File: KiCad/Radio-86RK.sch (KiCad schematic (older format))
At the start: 17 parts, among them SW67 Reset, U1 8080A/КР580ВМ80А, U12 74LS373/К555ИР22, U14 74LS138/К555ИД7, U16 7486/К155ЛП5, U17 7474/К155ТМ2, U18 7408/К155ЛИ1, U19 7404/К155ЛН1, U2 8224/КР580ГФ24, U20 7400/К155ЛА3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

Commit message: Change 8224 package to DIP16; Swap Down/Right keys; Fix U21 soviet designation
Signed-off-by: Sergey Kiselev <skiselev@gmail.com>
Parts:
- U2: footprint My_Components:IC_DIP20_300 -> My_Components:IC_DIP16_300
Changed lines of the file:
@@
 F 0 "U2" H 2100 2450 60  0000 L CNN
 F 1 "8224/КР580ГФ24" H 1600 2350 60  0000 L CNN
-F 2 "My_Components:IC_DIP20_300" H 2500 1600 60  0001 C CNN
+F 2 "My_Components:IC_DIP16_300" H 2500 1600 60  0001 C CNN
 F 3 "" H 2500 1600 60  0000 C CNN
 	1    2500 1650
@@
 Wire Wire Line
 	1700 1400 1800 1400
+$Comp
+L Device:C C44
+U 1 1 5F448F09
+P 1550 1400
+F 0 "C44" V 1600 1200 50  0000 L CNN
+F 1 "10pF" V 1600 1450 50  0000 L CNN
+F 2 "My_Components:Cap_Cer_508" H 1588 1250 50  0001 C CNN
+F 3 "" H 1550 1400 50  0000 C CNN
+	1    1550 1400
+	0    1    1    0
+$EndComp
 Wire Bus Line
-	9800 4600 9800 6100
+	6300 900  6300 4400
 Wire Bus Line
 	3400 4400 3400 5200
@@
 	4300 4500 4300 5700
 Wire Bus Line
-	6300 900  6300 4400
+	6100 2900 6100 4500
+Wire Bus Line
+	9800 4600 9800 6100
 Wire Bus Line
 	6100 900  6100 2500
-Wire Bus Line
-	6100 2900 6100 4500
-$Comp
-L Device:C C44
-U 1 1 5F448F09
-P 1550 1400
-F 0 "C44" V 1600 1200 50  0000 L CNN
-F 1 "10pF" V 1600 1450 50  0000 L CNN
-F 2 "My_Components:Cap_Cer_508" H 1588 1250 50  0001 C CNN
-F 3 "" H 1550 1400 50  0000 C CNN
-	1    1550 1400
-	0    1    1    0
-$EndComp
 $EndSCHEMATC

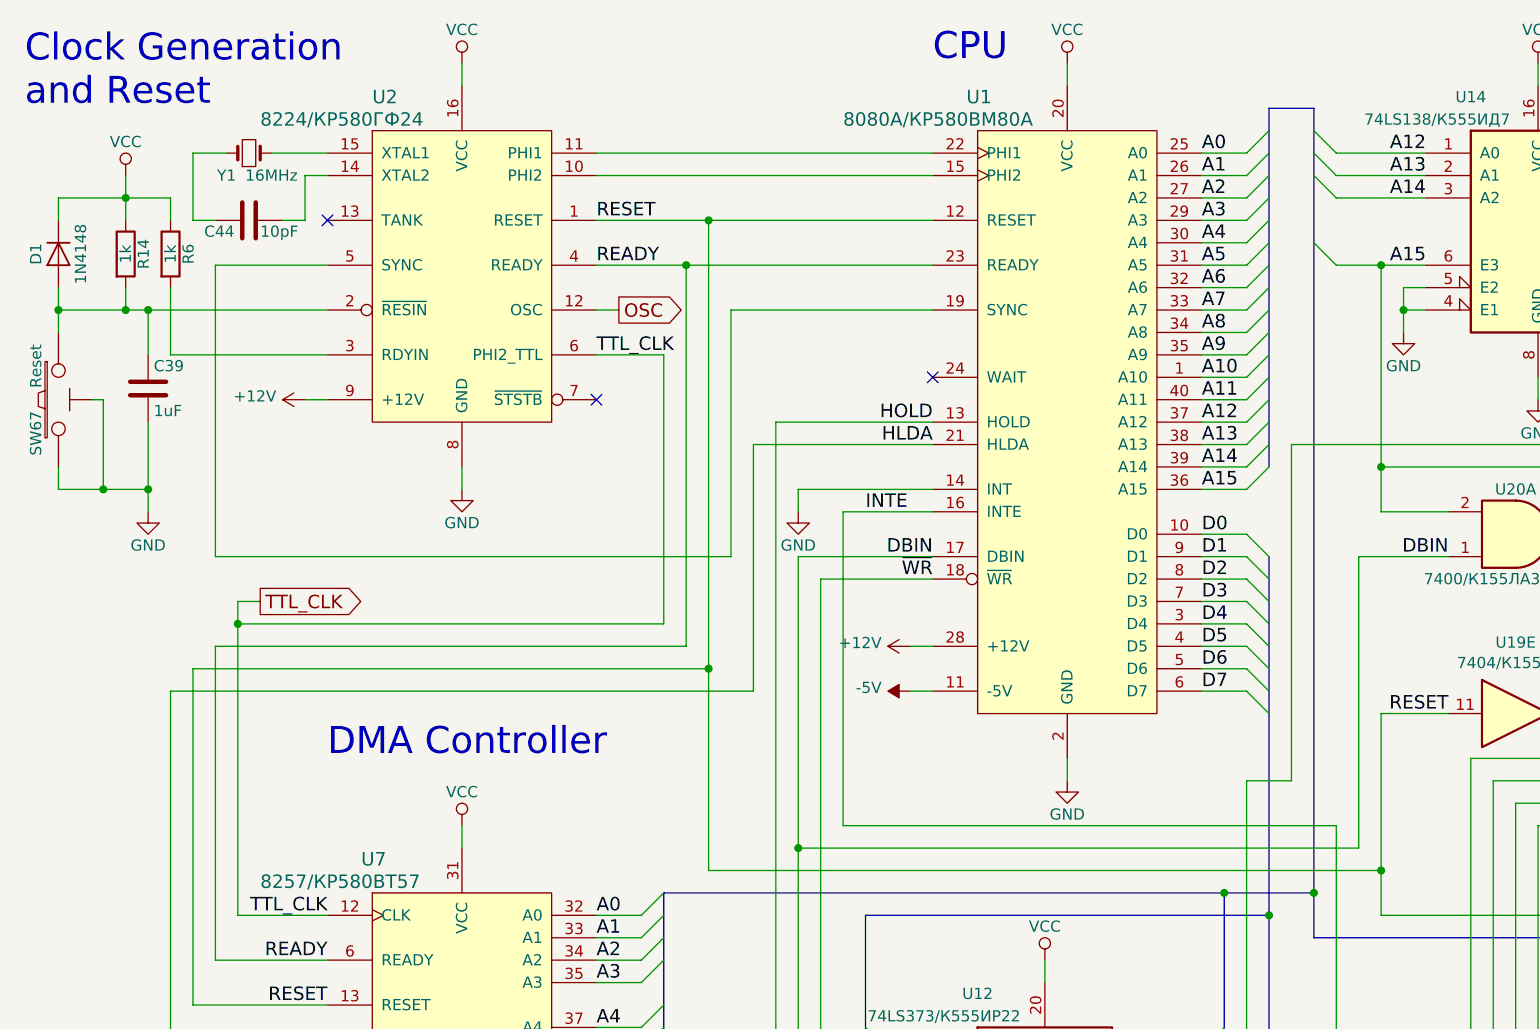
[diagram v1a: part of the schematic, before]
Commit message: Use DS1233 for reset
Signed-off-by: Sergey Kiselev <skiselev@gmail.com>
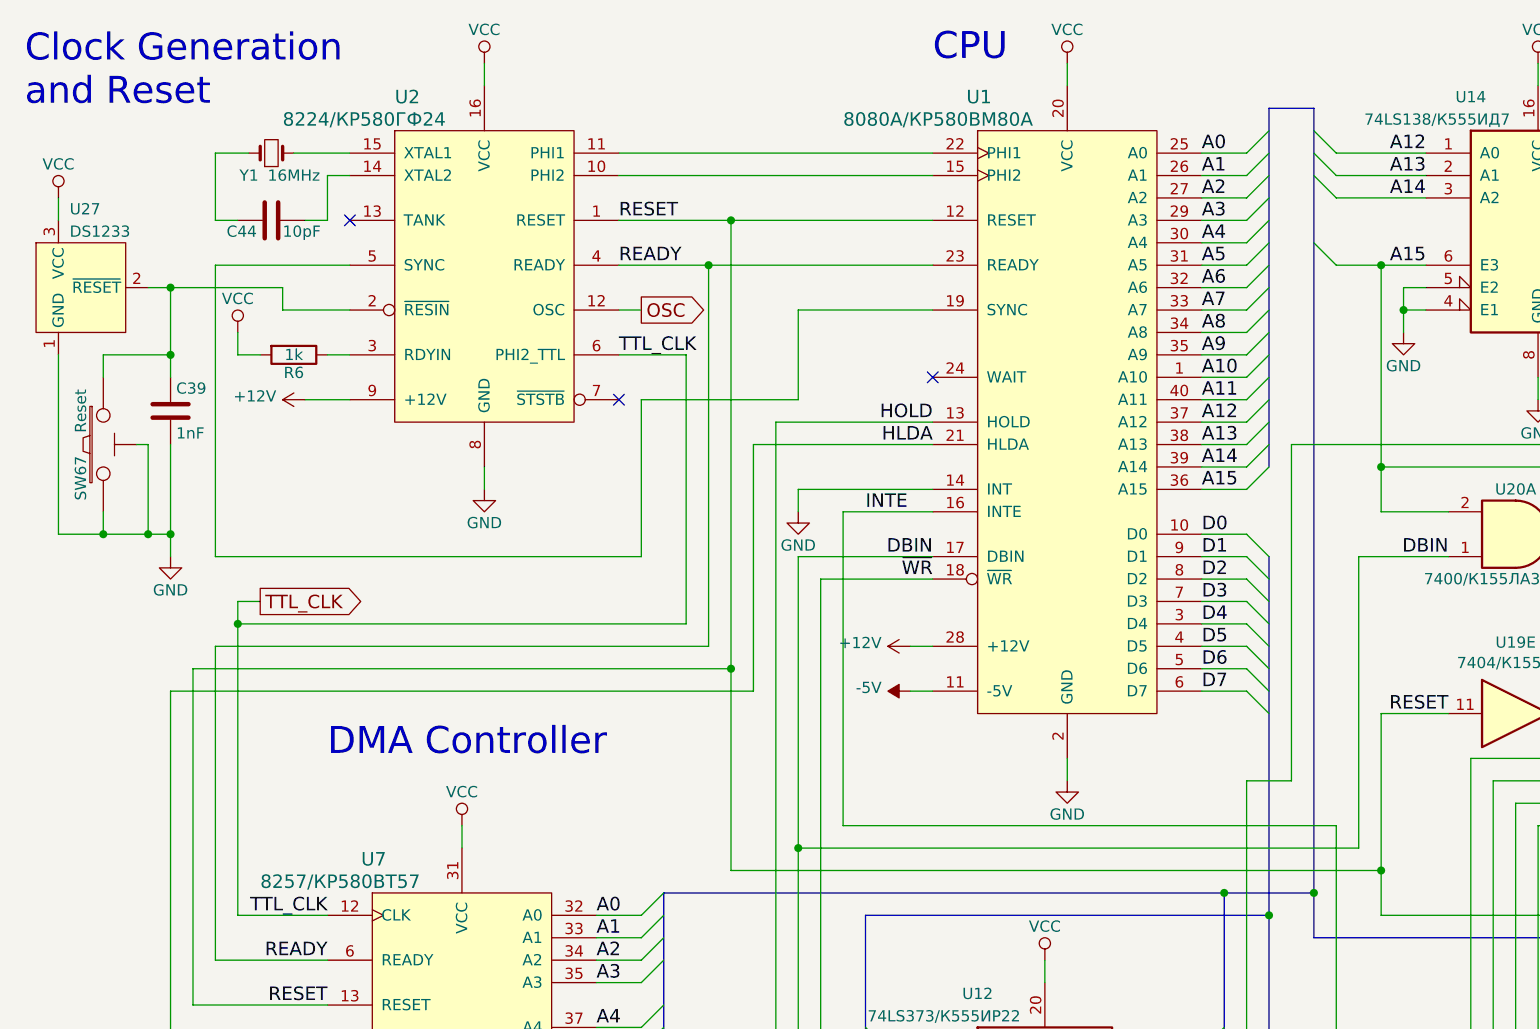
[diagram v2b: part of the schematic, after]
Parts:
- removed D1: 1N4148, My_Components:Diode_762, symbol Device:D
- removed R14: 1k, My_Components:Res_762, symbol Device:R
- added U27: DS1233, My_Components:Transistor_TO92_EBC_254, symbol my_components:DS1233
- C39: value 1uF -> 1nF
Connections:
- net GND: now also U27.1 (GND)
- net VCC: now also R6.2, U27.3 (VCC); no longer R6.1
- net at C39.1, SW67.1, U2.2 (~RESIN): now also U27.2 (~RESET)
- net at U2.3 (RDYIN): now also R6.1; no longer R6.2
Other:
- moved on the sheet: C39, C44, R6, SW67, U2, Y1

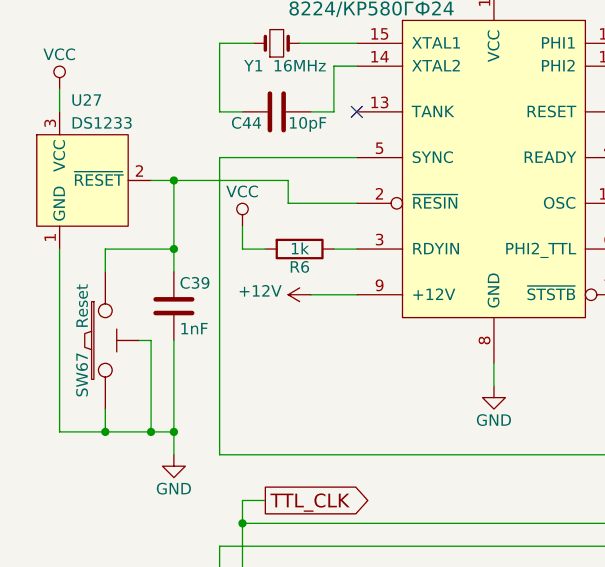
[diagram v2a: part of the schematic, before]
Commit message: Update design files to v1.1
Signed-off-by: Sergey Kiselev <skiselev@gmail.com>
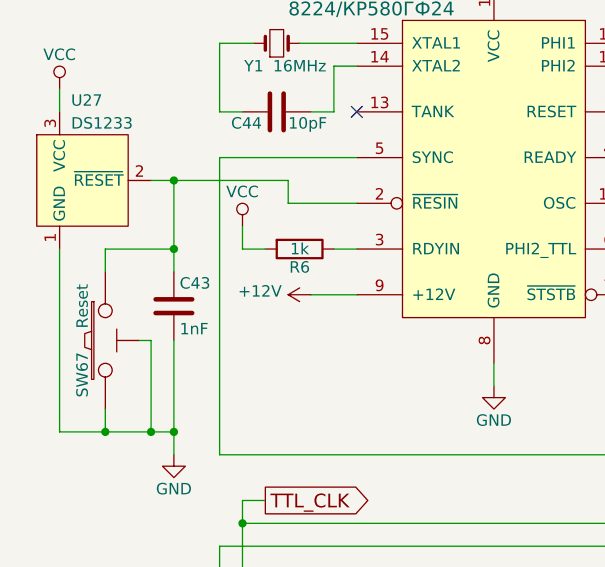
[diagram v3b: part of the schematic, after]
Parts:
- renumbered C39 to C43
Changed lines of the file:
@@
 $EndComp
 $Comp
-L Device:C C39
+L Device:C C43
 U 1 1 59322A46
 P 1200 2250
-F 0 "C39" H 1225 2350 50  0000 L CNN
+F 0 "C43" H 1225 2350 50  0000 L CNN
 F 1 "1nF" H 1225 2150 50  0000 L CNN
 F 2 "My_Components:Cap_Cer_508" H 1238 2100 50  0001 C CNN
